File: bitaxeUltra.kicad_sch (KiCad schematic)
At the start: 9 parts, among them J3 Barrel_Jack_Switch, M2 Fan_4pin

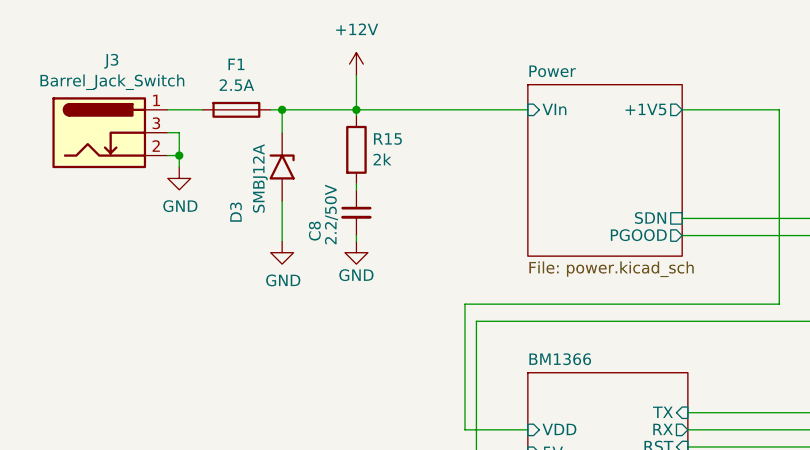
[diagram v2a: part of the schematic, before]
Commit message: removed useless snubber
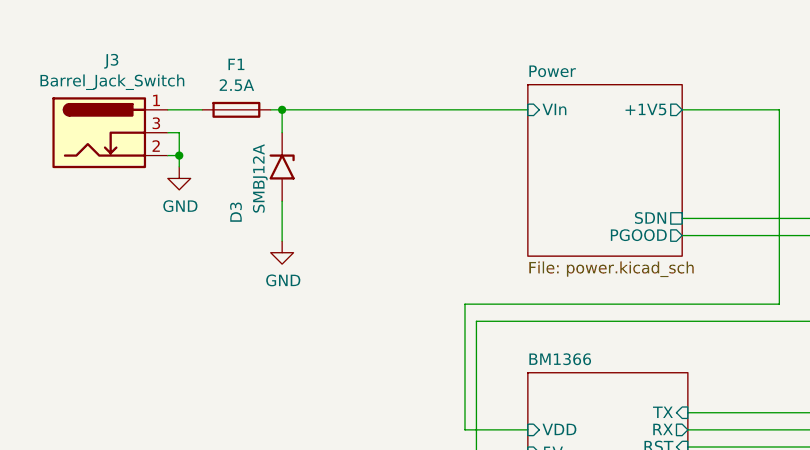
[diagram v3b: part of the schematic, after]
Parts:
- removed C8: 2.2/50V, Capacitor_SMD:C_1206_3216Metric, symbol Device:C_Small
- removed R15: 2k, Resistor_SMD:R_0805_2012Metric, symbol Device:R
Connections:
- net +12V: no longer D3.1 (A1), F1.1
- new net Power/VIn: D3.1 (A1), F1.1
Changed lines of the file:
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@@
   (junction (at 43.815 57.15) (diameter 0) (color 0 0 0 0)
-  )
-  (junction (at 63.5 52.07) (diameter 0) (color 0 0 0 0)
   )
   (no_connect (at 130.175 176.53))
@@
   (no_connect (at 122.555 186.69))
   (no_connect (at 122.555 181.61))
-  (wire (pts (xy 63.5 66.675) (xy 63.5 66.04))
-    (stroke (width 0) (type default))
-  )
   (wire (pts (xy 110.49 73.66) (xy 75.565 73.66))
     (stroke (width 0) (type default))
@@
     (stroke (width 0) (type default))
   )
-  (wire (pts (xy 63.5 52.07) (xy 63.5 52.705))
-    (stroke (width 0) (type default))
-  )
   (wire (pts (xy 100.33 87.63) (xy 144.78 87.63))
     (stroke (width 0) (type default))
@@
     (stroke (width 0) (type default))
   )
-  (wire (pts (xy 63.5 52.07) (xy 82.55 52.07))
-    (stroke (width 0) (type default))
-  )
   (wire (pts (xy 55.245 54.61) (xy 55.245 52.07))
     (stroke (width 0) (type default))
@@
     (stroke (width 0) (type default))
   )
-  (wire (pts (xy 63.5 48.26) (xy 63.5 52.07))
-    (stroke (width 0) (type default))
-  )
   (wire (pts (xy 100.33 85.725) (xy 144.78 85.725))
     (stroke (width 0) (type default))
@@
     (stroke (width 0) (type default))
   )
-  (wire (pts (xy 55.245 52.07) (xy 63.5 52.07))
-    (stroke (width 0) (type default))
-  )
-  (wire (pts (xy 63.5 60.96) (xy 63.5 60.325))
+  (wire (pts (xy 55.245 52.07) (xy 82.55 52.07))
     (stroke (width 0) (type default))
   )
@@
     )
   )
-  (symbol (lib_id "power:GND") (at 63.5 66.675 0) (unit 1)
-    (in_bom yes) (on_board yes) (dnp no)
-    (property "Reference" "#PWR022" (at 63.5 73.025 0)
-      (effects (font (size 1.27 1.27)) hide)
-    )
-    (property "Value" "GND" (at 63.5 70.485 0)
-      (effects (font (size 1.27 1.27)))
-    )
-    (property "Footprint" "" (at 63.5 66.675 0)
-      (effects (font (size 1.27 1.27)) hide)
-    )
-    (property "Datasheet" "" (at 63.5 66.675 0)
-      (effects (font (size 1.27 1.27)) hide)
-    )
-    (pin "1")
-    (instances
-      (project "pferdibank"
-        (path "/664662ce-7428-4243-a287-5a291ff0d522"
-          (reference "#PWR022") (unit 1)
-        )
-      )
-      (project "bitaxeUltra"
-        (path "/e63e39d7-6ac0-4ffd-8aa3-1841a4541b55/8ec0a9c6-2b78-44ef-a83d-9047d2828409"
-          (reference "#PWR011") (unit 1)
-        )
-        (path "/e63e39d7-6ac0-4ffd-8aa3-1841a4541b55"
-          (reference "#PWR011") (unit 1)
-        )
-      )
-    )
-  )
   (symbol (lib_id "Diode:5KPxxA") (at 55.245 58.42 270) (unit 1)
     (in_bom yes) (on_board yes) (dnp no)
@@
     )
   )
-  (symbol (lib_id "Device:R") (at 63.5 56.515 0) (unit 1)
-    (in_bom yes) (on_board yes) (dnp no)
-    (property "Reference" "R15" (at 65.278 55.3466 0)
-      (effects (font (size 1.27 1.27)) (justify left))
-    )
-    (property "Value" "2k" (at 65.278 57.658 0)
-      (effects (font (size 1.27 1.27)) (justify left))
-    )
-    (property "Footprint" "Resistor_SMD:R_0805_2012Metric" (at 61.722 56.515 90)
-      (effects (font (size 1.27 1.27)) hide)
-    )
-    (property "Datasheet" "~" (at 63.5 56.515 0)
-      (effects (font (size 1.27 1.27)) hide)
-    )
-    (pin "1")
-    (pin "2")
-    (instances
-      (project "pferdibank"
-        (path "/664662ce-7428-4243-a287-5a291ff0d522"
-          (reference "R15") (unit 1)
-        )
-      )
-      (project "bitaxeUltra"
-        (path "/e63e39d7-6ac0-4ffd-8aa3-1841a4541b55/8ec0a9c6-2b78-44ef-a83d-9047d2828409"
-          (reference "R12") (unit 1)
-        )
-        (path "/e63e39d7-6ac0-4ffd-8aa3-1841a4541b55"
-          (reference "R10") (unit 1)
-        )
-      )
-    )
-  )
-  (symbol (lib_id "power:+12V") (at 63.5 48.26 0) (unit 1)
-    (in_bom yes) (on_board yes) (dnp no) (fields_autoplaced)
-    (property "Reference" "#PWR09" (at 63.5 52.07 0)
-      (effects (font (size 1.27 1.27)) hide)
-    )
-    (property "Value" "+12V" (at 63.5 43.18 0)
-      (effects (font (size 1.27 1.27)))
-    )
-    (property "Footprint" "" (at 63.5 48.26 0)
-      (effects (font (size 1.27 1.27)) hide)
-    )
-    (property "Datasheet" "" (at 63.5 48.26 0)
-      (effects (font (size 1.27 1.27)) hide)
-    )
-    (pin "1")
-    (instances
-      (project "bitaxeUltra"
-        (path "/e63e39d7-6ac0-4ffd-8aa3-1841a4541b55/8ec0a9c6-2b78-44ef-a83d-9047d2828409"
-          (reference "#PWR09") (unit 1)
-        )
-        (path "/e63e39d7-6ac0-4ffd-8aa3-1841a4541b55"
-          (reference "#PWR09") (unit 1)
-        )
-      )
-    )
-  )
   (symbol (lib_id "power:+12V") (at 32.385 182.88 180) (unit 1)
     (in_bom yes) (on_board yes) (dnp no) (fields_autoplaced)
@@
         )
       )
-    )
-  )
-  (symbol (lib_id "Device:C_Small") (at 63.5 63.5 0) (unit 1)
-    (in_bom yes) (on_board yes) (dnp no)
-    (property "Reference" "C8" (at 58.928 65.532 90)
-      (effects (font (size 1.27 1.27)))
-    )
-    (property "Value" "2.2/50V" (at 60.706 63.754 90)
-      (effects (font (size 1.27 1.27)))
-    )
-    (property "Footprint" "Capacitor_SMD:C_1206_3216Metric" (at 63.5 63.5 0)
-      (effects (font (size 1.27 1.27)) hide)
-    )
-    (property "Datasheet" "~" (at 63.5 63.5 0)
-      (effects (font (size 1.27 1.27)) hide)
-    )
-    (property "Distributor" "" (at 63.5 63.5 0)
-      (effects (font (size 1.27 1.27)) hide)
-    )
-    (property "Manufacturer" "" (at 63.5 63.5 0)
-      (effects (font (size 1.27 1.27)) hide)
-    )
-    (property "OrderNr" "" (at 63.5 63.5 0)
-      (effects (font (size 1.27 1.27)) hide)
-    )
-    (pin "1")
-    (pin "2")
-    (instances
-      (project "pferdibank"
-        (path "/664662ce-7428-4243-a287-5a291ff0d522"
-          (reference "C8") (unit 1)
-        )
-      )
-      (project "bitaxeUltra"
-        (path "/e63e39d7-6ac0-4ffd-8aa3-1841a4541b55/8ec0a9c6-2b78-44ef-a83d-9047d2828409"
-          (reference "C34") (unit 1)
-        )
-        (path "/e63e39d7-6ac0-4ffd-8aa3-1841a4541b55"
-          (reference "C26") (unit 1)
-        )
-      )
